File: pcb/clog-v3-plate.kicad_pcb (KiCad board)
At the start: 2 copper layers, 125.3 x 81.8 mm, 22 parts, among them SW1 SW_Push, SW10 SW_Push, SW11 SW_Push, SW12 SW_Push, SW13 SW_Push, SW14 SW_Push, SW15 SW_Push, SW16 SW_Push, SW17 SW_Push, SW2 SW_Push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

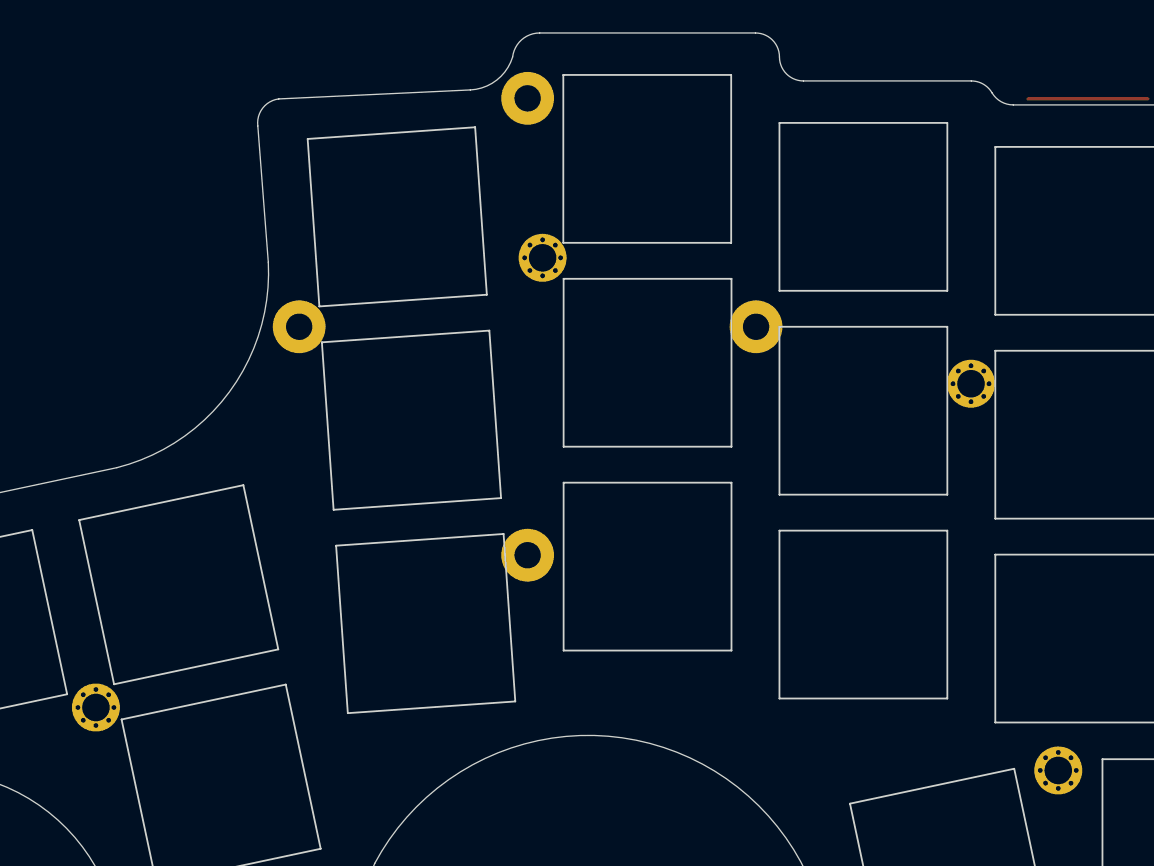
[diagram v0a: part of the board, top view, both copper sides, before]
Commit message: Update Reset Switch, Remove Holes From Plate
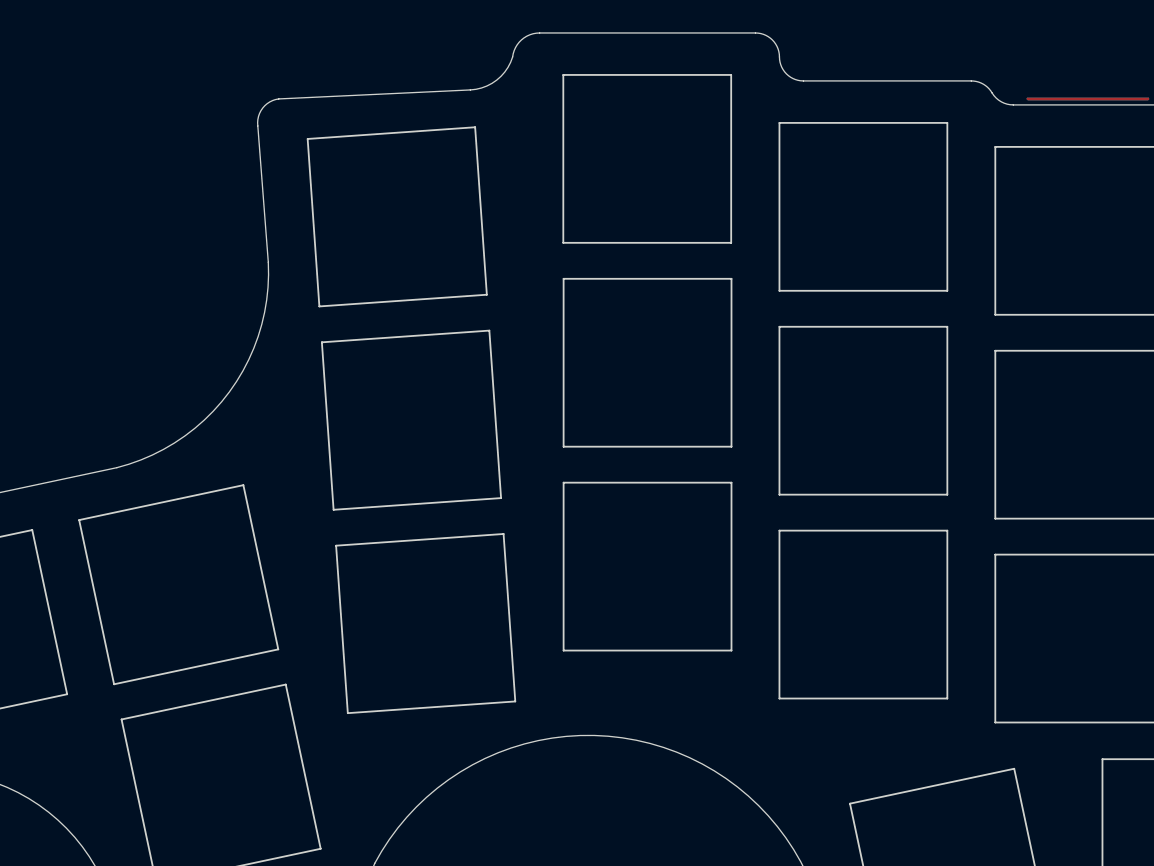
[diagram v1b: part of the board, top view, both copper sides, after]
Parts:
- removed REF**: Tenting Puck, footprints:tenting-puck
- removed Ref** (x4): Val**, footprints:m2-hole
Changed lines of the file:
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@@
     (fp_line (start 7 -7) (end -7 -7) (layer "Edge.Cuts") (width 0.15))
-  )
-  (footprint "footprints:m2-hole" (layer "F.Cu")
-    (at 180.25 87)
-    (descr "Mounting Hole 2.2mm, no annular, M2")
-    (tags "mounting hole 2.2mm no annular m2")
-    (attr exclude_from_pos_files exclude_from_bom)
-    (fp_text reference "Ref**" (at 0 0) (layer "F.SilkS") hide
-      (effects (font (size 1.27 1.27) (thickness 0.15)))
-    )
-    (fp_text value "Val**" (at 0 0) (layer "F.SilkS") hide
-      (effects (font (size 1.27 1.27) (thickness 0.15)))
-    )
-    (fp_circle (center 0 0) (end 2.2 0) (layer "Cmts.User") (width 0.15) (fill none))
-    (fp_circle (center 0 0) (end 2.45 0) (layer "F.CrtYd") (width 0.05) (fill none))
-    (pad "1" thru_hole circle (at 1.06 -1.06) (size 0.5 0.5) (drill 0.4) (layers *.Cu *.Mask))
-    (pad "1" thru_hole circle (at 0 -1.5) (size 0.5 0.5) (drill 0.4) (layers *.Cu *.Mask))
-    (pad "1" thru_hole circle (at 1.06 1.06) (size 0.5 0.5) (drill 0.4) (layers *.Cu *.Mask))
-    (pad "1" thru_hole circle (at -1.06 -1.06) (size 0.5 0.5) (drill 0.4) (layers *.Cu *.Mask))
-    (pad "1" thru_hole circle (at -1.5 0) (size 0.5 0.5) (drill 0.4) (layers *.Cu *.Mask))
-    (pad "1" thru_hole circle (at 0 0) (size 4 4) (drill 2.3) (layers *.Cu *.Mask))
-    (pad "1" thru_hole circle (at 0 1.5) (size 0.5 0.5) (drill 0.4) (layers *.Cu *.Mask))
-    (pad "1" thru_hole circle (at -1.06 1.06) (size 0.5 0.5) (drill 0.4) (layers *.Cu *.Mask))
-    (pad "1" thru_hole circle (at 1.5 0) (size 0.5 0.5) (drill 0.4) (layers *.Cu *.Mask))
-  )
-  (footprint "footprints:m2-hole" (layer "F.Cu")
-    (at 144.524999 76.500002)
-    (descr "Mounting Hole 2.2mm, no annular, M2")
-    (tags "mounting hole 2.2mm no annular m2")
-    (attr exclude_from_pos_files exclude_from_bom)
-    (fp_text reference "Ref**" (at 0 0) (layer "F.SilkS") hide
-      (effects (font (size 1.27 1.27) (thickness 0.15)))
-    )
-    (fp_text value "Val**" (at 0 0) (layer "F.SilkS") hide
-      (effects (font (size 1.27 1.27) (thickness 0.15)))
-    )
-    (fp_circle (center 0 0) (end 2.2 0) (layer "Cmts.User") (width 0.15) (fill none))
-    (fp_circle (center 0 0) (end 2.45 0) (layer "F.CrtYd") (width 0.05) (fill none))
-    (pad "1" thru_hole circle (at 1.06 1.06) (size 0.5 0.5) (drill 0.4) (layers *.Cu *.Mask))
-    (pad "1" thru_hole circle (at -1.06 -1.06) (size 0.5 0.5) (drill 0.4) (layers *.Cu *.Mask))
-    (pad "1" thru_hole circle (at -1.5 0) (size 0.5 0.5) (drill 0.4) (layers *.Cu *.Mask))
-    (pad "1" thru_hole circle (at 0 1.5) (size 0.5 0.5) (drill 0.4) (layers *.Cu *.Mask))
-    (pad "1" thru_hole circle (at 0 0) (size 4 4) (drill 2.3) (layers *.Cu *.Mask))
-    (pad "1" thru_hole circle (at 1.06 -1.06) (size 0.5 0.5) (drill 0.4) (layers *.Cu *.Mask))
-    (pad "1" thru_hole circle (at 0 -1.5) (size 0.5 0.5) (drill 0.4) (layers *.Cu *.Mask))
-    (pad "1" thru_hole circle (at 1.5 0) (size 0.5 0.5) (drill 0.4) (layers *.Cu *.Mask))
-    (pad "1" thru_hole circle (at -1.06 1.06) (size 0.5 0.5) (drill 0.4) (layers *.Cu *.Mask))
-  )
-  (footprint "footprints:m2-hole" (layer "F.Cu")
-    (at 187.524999 119.250002)
-    (descr "Mounting Hole 2.2mm, no annular, M2")
-    (tags "mounting hole 2.2mm no annular m2")
-    (attr exclude_from_pos_files exclude_from_bom)
-    (fp_text reference "Ref**" (at 0 0) (layer "F.SilkS") hide
-      (effects (font (size 1.27 1.27) (thickness 0.15)))
-    )
-    (fp_text value "Val**" (at 0 0) (layer "F.SilkS") hide
-      (effects (font (size 1.27 1.27) (thickness 0.15)))
-    )
-    (fp_circle (center 0 0) (end 2.2 0) (layer "Cmts.User") (width 0.15) (fill none))
-    (fp_circle (center 0 0) (end 2.45 0) (layer "F.CrtYd") (width 0.05) (fill none))
-    (pad "1" thru_hole circle (at -1.06 1.06) (size 0.5 0.5) (drill 0.4) (layers *.Cu *.Mask))
-    (pad "1" thru_hole circle (at -1.5 0) (size 0.5 0.5) (drill 0.4) (layers *.Cu *.Mask))
-    (pad "1" thru_hole circle (at -1.06 -1.06) (size 0.5 0.5) (drill 0.4) (layers *.Cu *.Mask))
-    (pad "1" thru_hole circle (at 1.06 -1.06) (size 0.5 0.5) (drill 0.4) (layers *.Cu *.Mask))
-    (pad "1" thru_hole circle (at 1.5 0) (size 0.5 0.5) (drill 0.4) (layers *.Cu *.Mask))
-    (pad "1" thru_hole circle (at 0 -1.5) (size 0.5 0.5) (drill 0.4) (layers *.Cu *.Mask))
-    (pad "1" thru_hole circle (at 0 1.5) (size 0.5 0.5) (drill 0.4) (layers *.Cu *.Mask))
-    (pad "1" thru_hole circle (at 0 0) (size 4 4) (drill 2.3) (layers *.Cu *.Mask))
-    (pad "1" thru_hole circle (at 1.06 1.06) (size 0.5 0.5) (drill 0.4) (layers *.Cu *.Mask))
-  )
-  (footprint "footprints:m2-hole" (layer "F.Cu")
-    (at 107.274999 114.000002)
-    (descr "Mounting Hole 2.2mm, no annular, M2")
-    (tags "mounting hole 2.2mm no annular m2")
-    (attr exclude_from_pos_files exclude_from_bom)
-    (fp_text reference "Ref**" (at 0 0) (layer "F.SilkS") hide
-      (effects (font (size 1.27 1.27) (thickness 0.15)))
-    )
-    (fp_text value "Val**" (at 0 0) (layer "F.SilkS") hide
-      (effects (font (size 1.27 1.27) (thickness 0.15)))
-    )
-    (fp_circle (center 0 0) (end 2.2 0) (layer "Cmts.User") (width 0.15) (fill none))
-    (fp_circle (center 0 0) (end 2.45 0) (layer "F.CrtYd") (width 0.05) (fill none))
-    (pad "1" thru_hole circle (at -1.06 1.06) (size 0.5 0.5) (drill 0.4) (layers *.Cu *.Mask))
-    (pad "1" thru_hole circle (at 1.5 0) (size 0.5 0.5) (drill 0.4) (layers *.Cu *.Mask))
-    (pad "1" thru_hole circle (at 0 1.5) (size 0.5 0.5) (drill 0.4) (layers *.Cu *.Mask))
-    (pad "1" thru_hole circle (at -1.5 0) (size 0.5 0.5) (drill 0.4) (layers *.Cu *.Mask))
-    (pad "1" thru_hole circle (at -1.06 -1.06) (size 0.5 0.5) (drill 0.4) (layers *.Cu *.Mask))
-    (pad "1" thru_hole circle (at 0 0) (size 4 4) (drill 2.3) (layers *.Cu *.Mask))
-    (pad "1" thru_hole circle (at 0 -1.5) (size 0.5 0.5) (drill 0.4) (layers *.Cu *.Mask))
-    (pad "1" thru_hole circle (at 1.06 -1.06) (size 0.5 0.5) (drill 0.4) (layers *.Cu *.Mask))
-    (pad "1" thru_hole circle (at 1.06 1.06) (size 0.5 0.5) (drill 0.4) (layers *.Cu *.Mask))
   )
   (footprint "footprints:choc-cutout" (layer "F.Cu")
@@
     (fp_line (start 7 -7) (end -7 -7) (layer "Edge.Cuts") (width 0.15))
   )
-  (footprint "footprints:tenting-puck" (layer "F.Cu")
-    (at 143.274999 82.250002)
-    (descr "https://splitkb.com/products/tenting-puck")
-    (tags "split kb tenting puck mechanical mounting")
-    (attr through_hole exclude_from_pos_files exclude_from_bom)
-    (fp_text reference "REF**" (at 7.6835 1.4605) (layer "F.Fab") hide
-      (effects (font (size 1 1) (thickness 0.15)))
-    )
-    (fp_text value "Tenting Puck" (at 8.0645 -2.8575) (layer "F.Fab") hide
-      (effects (font (size 1 1) (thickness 0.15)))
-    )
-    (pad "1" thru_hole circle (at 19.05 0) (size 4.4 4.4) (drill 2.2) (layers *.Cu *.Mask))
-    (pad "1" thru_hole circle (at 0 19.05) (size 4.4 4.4) (drill 2.2) (layers *.Cu *.Mask))
-    (pad "1" thru_hole circle (at 0 -19.05) (size 4.4 4.4) (drill 2.2) (layers *.Cu *.Mask))
-    (pad "1" thru_hole circle (at -19.05 0) (size 4.4 4.4) (drill 2.2) (layers *.Cu *.Mask))
-  )
-  (footprint "footprints:choc-cutout" (layer "F.Cu")
+  (footprint "footprints:choc-cutout" (layer "F.Cu")

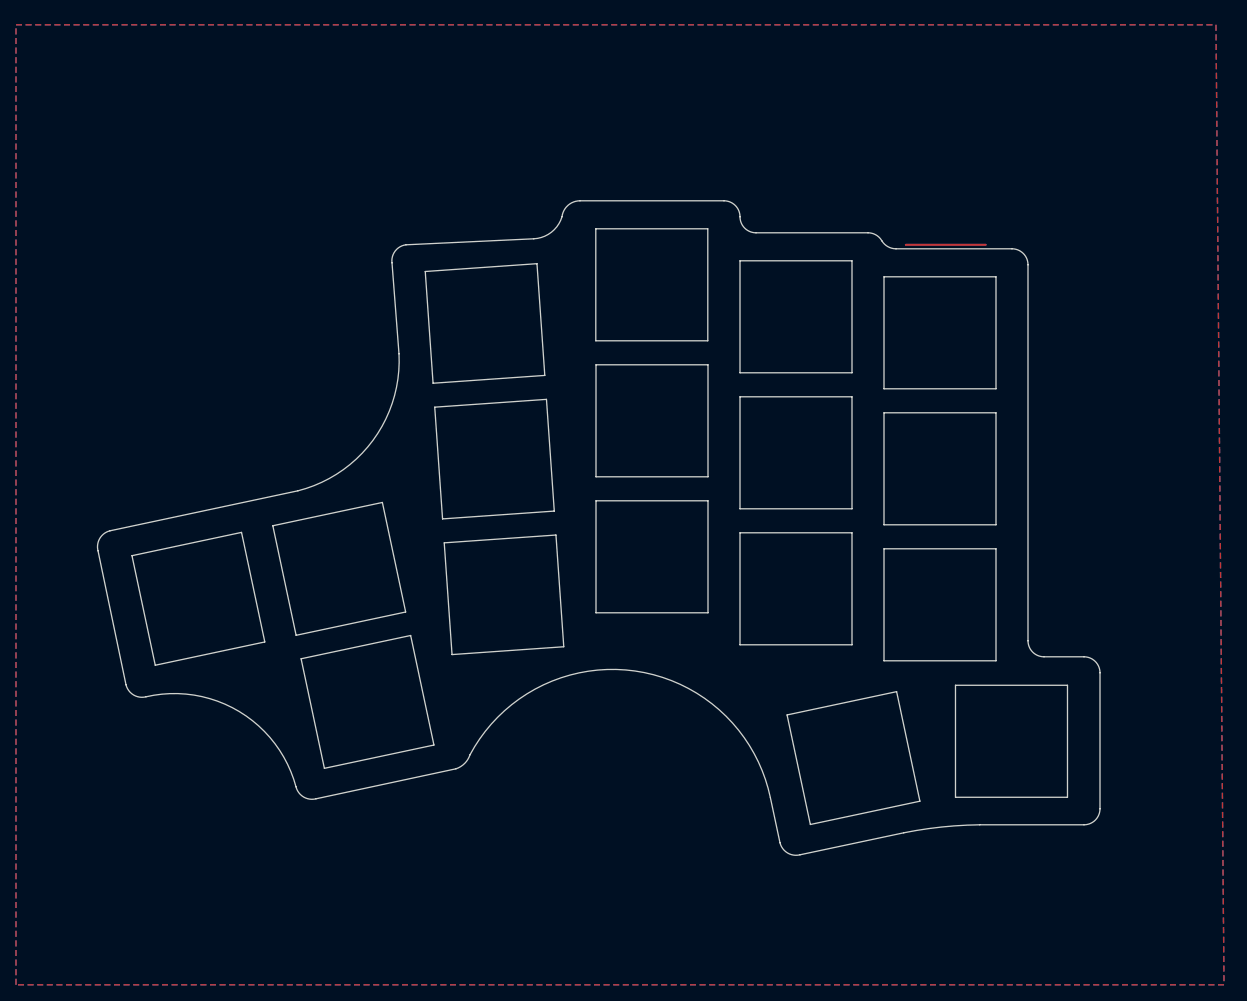
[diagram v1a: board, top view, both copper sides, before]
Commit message: Move Pinky Further Up, Rotate Thumbs Out
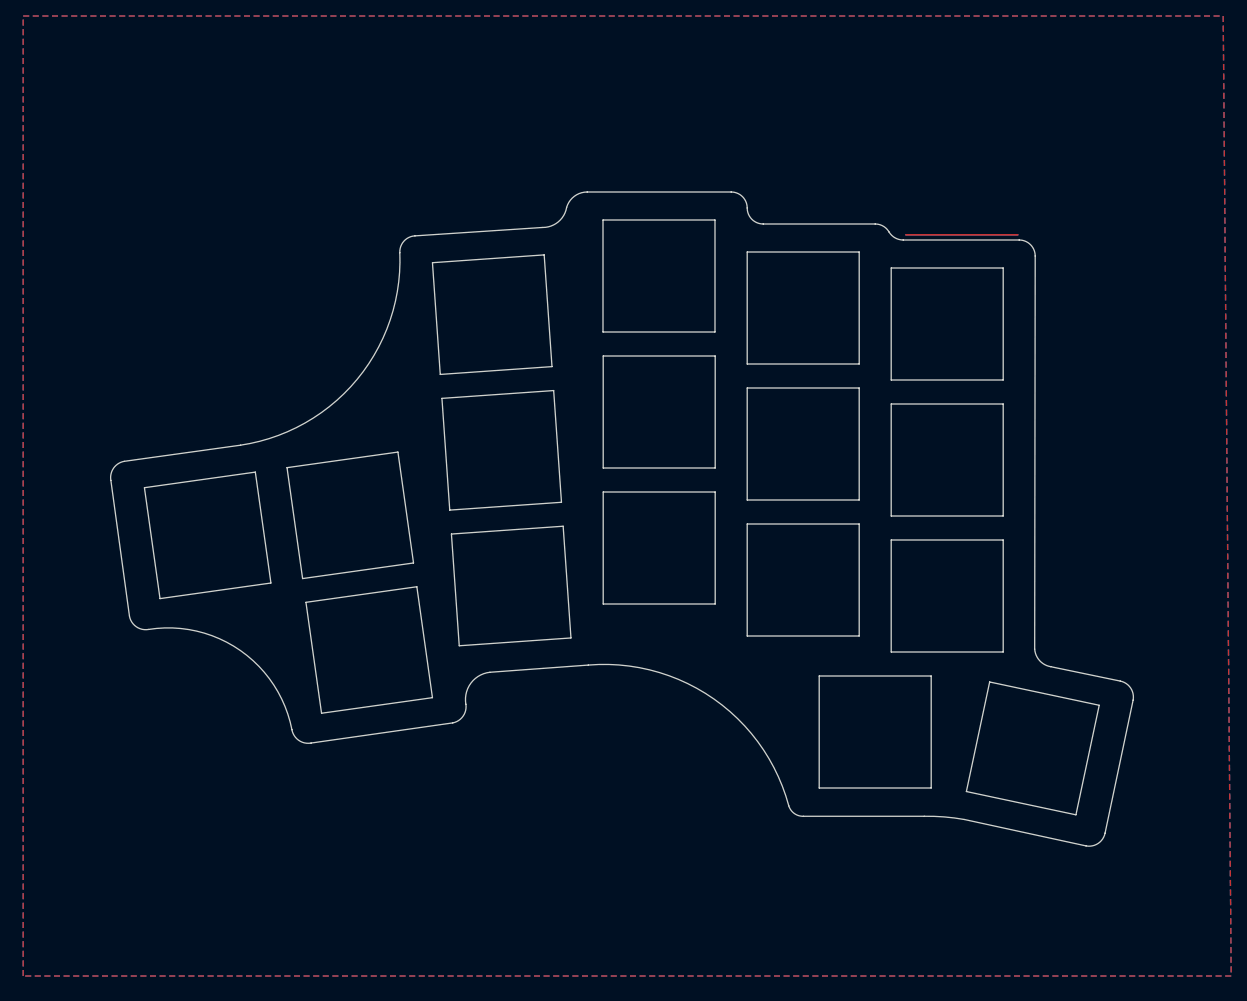
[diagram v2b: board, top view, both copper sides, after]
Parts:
- moved SW5 8.02 mm to (97.7, 99.6), turned to 8 degrees
- moved SW6 6.84 mm to (115.6, 97.1), turned to 8 degrees
- moved SW11 6.49 mm to (117.9, 113.9), turned to 8 degrees
- moved SW16 4.24 mm to (181.2, 124.2), turned to 0 degrees
- moved SW17 2.81 mm to (200.9, 126.2), turned to -12 degrees
- moved SW3 1.42 mm to (172.2, 71.2)
- moved SW12 1.42 mm to (135.7, 105.9)
- moved SW1 1.42 mm to (133.3, 72.0)
- moved SW4 1.42 mm to (190.2, 73.2)
- moved SW8 1.42 mm to (154.2, 84.2)
- moved SW10 1.42 mm to (190.2, 90.2)
- moved SW2 1.42 mm to (154.2, 67.2)
- moved SW13 1.42 mm to (154.2, 101.2)
- moved SW7 1.42 mm to (134.5, 88.9)
- moved SW15 1.42 mm to (190.2, 107.2)
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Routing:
- net (no net): track 10.0 -> 0.00 mm
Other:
- board size 125.3 x 81.8 mm -> 127.8 x 81.8 mm
